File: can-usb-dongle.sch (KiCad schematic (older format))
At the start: 42 parts, among them SW1 SW_PUSH, U1 STM32F302C8T, U2 SN65HVD256, U3 NUF2042XV6, U4 MCP1700, U5 SiP32431, X1 16MHz 10ppm

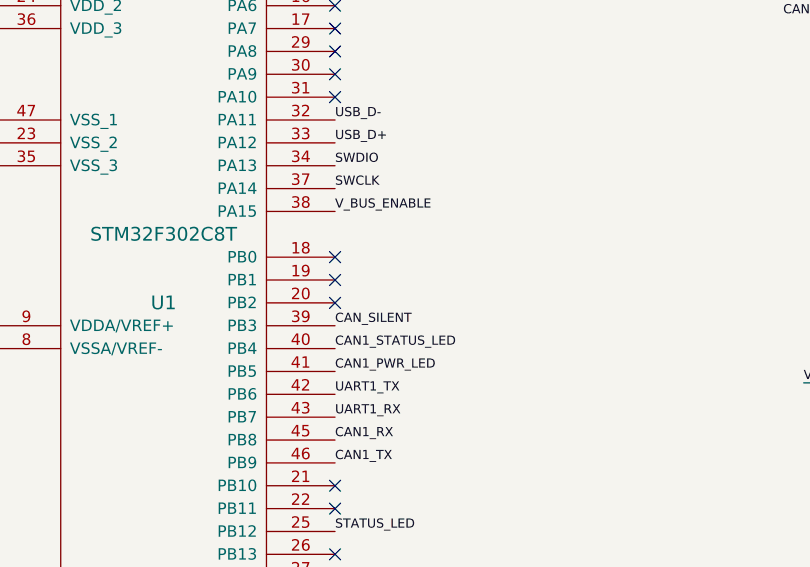
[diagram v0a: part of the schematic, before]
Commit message: Resolve GPIO conflict with JTAG pin
V_BUS_ENABLE and CAN_SILENT were in conflict with JTAG output pins.
They had to be moved because at boot time the output value cannot be guaranteed.
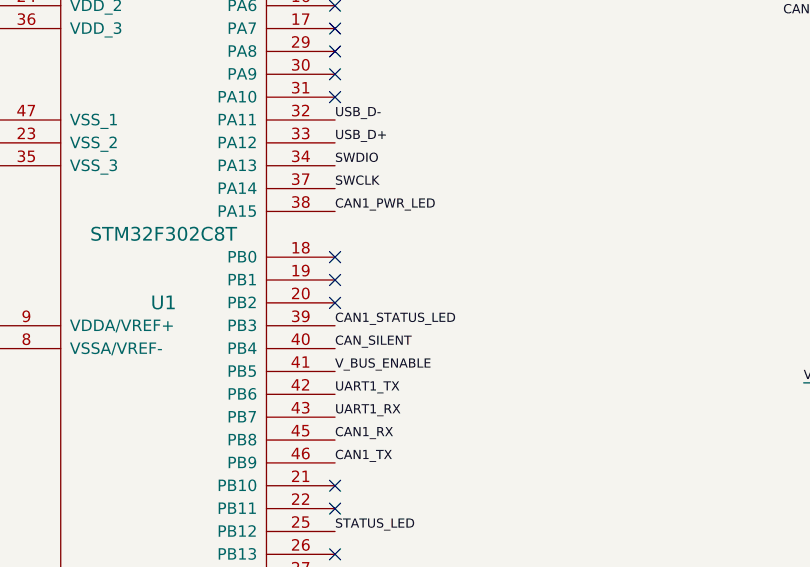
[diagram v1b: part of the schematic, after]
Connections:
- net CAN1_PWR_LED: now also U1.38 (PA15); no longer U1.41 (PB5)
- net CAN1_STATUS_LED: now also U1.39 (PB3); no longer U1.40 (PB4)
- net CAN_SILENT: now also U1.40 (PB4); no longer U1.39 (PB3)
- net V_BUS_ENABLE: now also U1.41 (PB5); no longer U1.38 (PA15)
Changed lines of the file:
@@
 Text Label 6000 1450 2    40   ~ 0
 STATUS_LED
-Text Label 3600 3500 0    40   ~ 0
+Text Label 3600 3400 0    40   ~ 0
 CAN1_STATUS_LED
 $Comp
@@
 	1    0    0    -1
 $EndComp
-Text Label 3600 3400 0    40   ~ 0
+Text Label 3600 3500 0    40   ~ 0
 CAN_SILENT
 Text Label 3600 3800 0    40   ~ 0
@@
 Text Label 8100 2250 0    40   ~ 0
 V_BUS_ENABLE
-Text Label 3600 2900 0    40   ~ 0
+Text Label 3600 3600 0    40   ~ 0
 V_BUS_ENABLE
 $Comp
@@
 Text Label 6000 2050 2    40   ~ 0
 CAN1_PWR_LED
-Text Label 3600 3600 0    40   ~ 0
+Text Label 3600 2900 0    40   ~ 0
 CAN1_PWR_LED
 Text Label 6000 1750 2    40   ~ 0

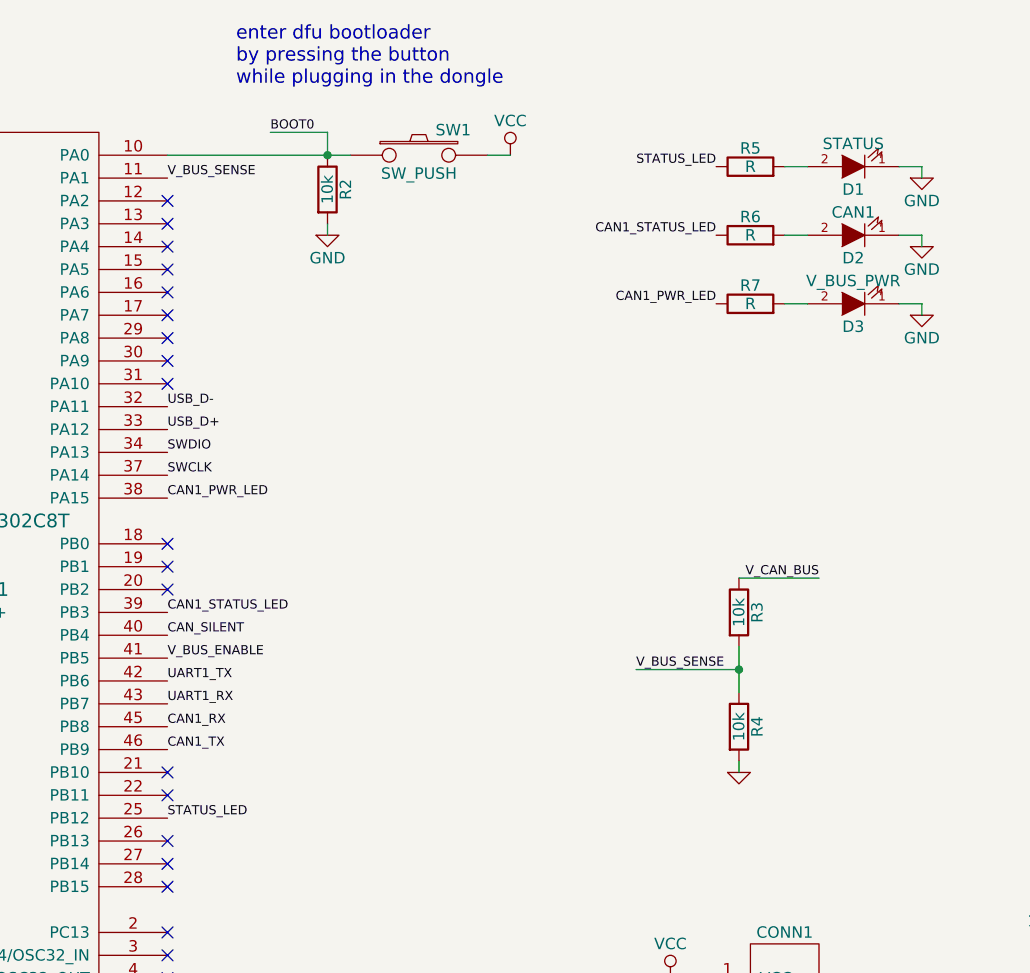
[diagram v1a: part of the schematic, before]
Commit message: Resolve JTAG pin conflict, add V_BUS_SENSE filter cap
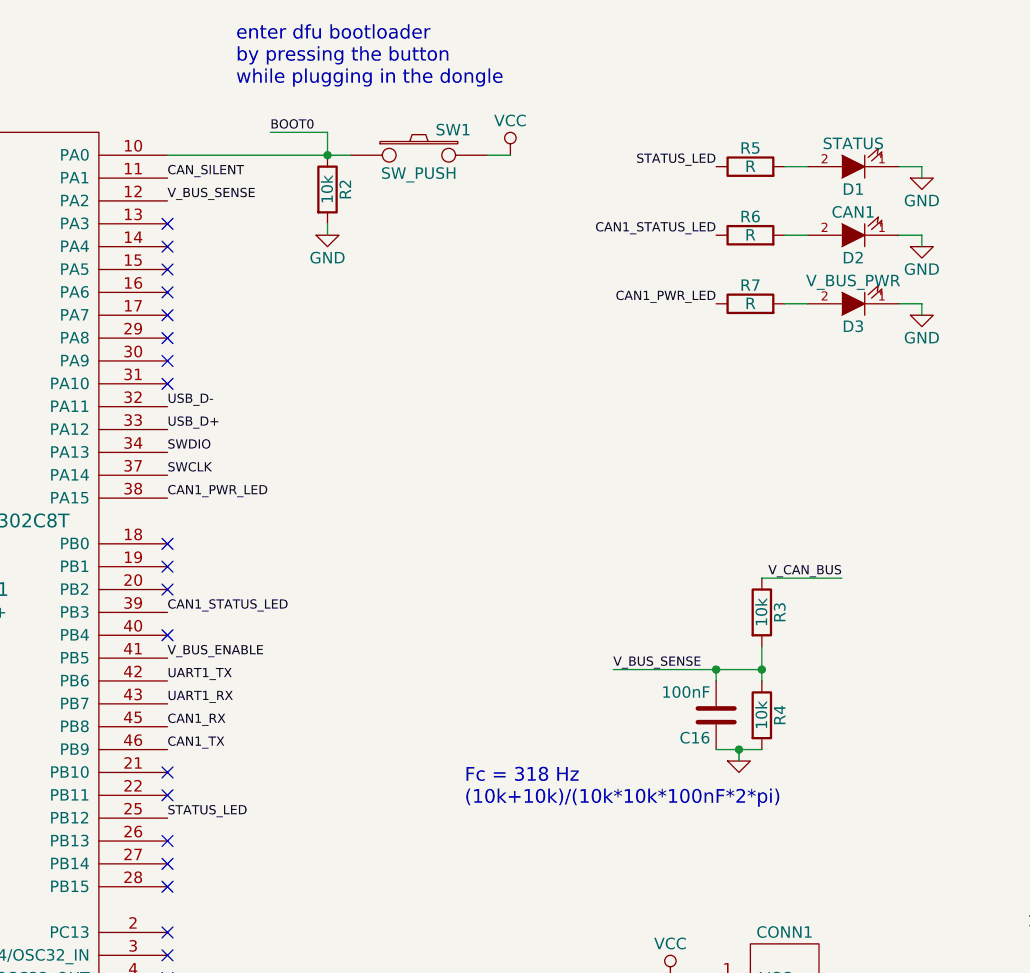
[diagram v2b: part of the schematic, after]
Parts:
- added C16: 100nF, _std:_0603, symbol C
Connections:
- net CAN_SILENT: now also U1.11 (PA1); no longer U1.40 (PB4)
- net GND: now also C16.1
- net V_BUS_SENSE: now also U1.12 (PA2), C16.2; no longer U1.11 (PA1)
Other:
- note added: "Fc = 318 Hz\n(10k+10k)/(10k*10k*100nF*2*pi)"
- moved on the sheet: R3, R4
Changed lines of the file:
@@
 	1    0    0    -1
 $EndComp
-Text Label 3600 3500 0    40   ~ 0
+Text Label 3600 1500 0    40   ~ 0
 CAN_SILENT
 Text Label 3600 3800 0    40   ~ 0
@@
 NoConn ~ 3600 2300
 NoConn ~ 3600 1700
-NoConn ~ 3600 1600
 $Comp
 L CAN CONN5
@@
 	1    0    0    -1
 $EndComp
-Text Label 6450 3250 2    40   ~ 0
+Text Label 6550 3250 2    40   ~ 0
 V_CAN_BUS
 $Comp
 L R R3
 U 1 1 560BE6FC
-P 6100 3400
-F 0 "R3" V 6180 3400 50  0000 C CNN
-F 1 "10k" V 6100 3400 50  0000 C CNN
-F 2 "_std:_0603" V 6030 3400 30  0001 C CNN
-F 3 "" H 6100 3400 30  0000 C CNN
-	1    6100 3400
+P 6200 3400
+F 0 "R3" V 6280 3400 50  0000 C CNN
+F 1 "10k" V 6200 3400 50  0000 C CNN
+F 2 "_std:_0603" V 6130 3400 30  0001 C CNN
+F 3 "" H 6200 3400 30  0000 C CNN
+	1    6200 3400
 	1    0    0    -1
 $EndComp
@@
 L R R4
 U 1 1 560BE79F
-P 6100 3900
-F 0 "R4" V 6180 3900 50  0000 C CNN
-F 1 "10k" V 6100 3900 50  0000 C CNN
-F 2 "_std:_0603" V 6030 3900 30  0001 C CNN
-F 3 "" H 6100 3900 30  0000 C CNN
-	1    6100 3900
+P 6200 3850
+F 0 "R4" V 6280 3850 50  0000 C CNN
+F 1 "10k" V 6200 3850 50  0000 C CNN
+F 2 "_std:_0603" V 6130 3850 30  0001 C CNN
+F 3 "" H 6200 3850 30  0000 C CNN
+	1    6200 3850
 	1    0    0    -1
 $EndComp
@@
 L GND-RESCUE-can-usb-dongle #PWR026
 U 1 1 560BE823
-P 6100 4100
-F 0 "#PWR026" H 6100 4100 30  0001 C CNN
-F 1 "GND" H 6100 4030 30  0001 C CNN
-F 2 "" H 6100 4100 60  0000 C CNN
-F 3 "" H 6100 4100 60  0000 C CNN
-	1    6100 4100
-	1    0    0    -1
-$EndComp
-Text Label 5650 3650 0    40   ~ 0
+P 6100 4050
+F 0 "#PWR026" H 6100 4050 30  0001 C CNN
+F 1 "GND" H 6100 3980 30  0001 C CNN
+F 2 "" H 6100 4050 60  0000 C CNN
+F 3 "" H 6100 4050 60  0000 C CNN
+	1    6100 4050
+	1    0    0    -1
+$EndComp
+Text Label 5550 3650 0    40   ~ 0
 V_BUS_SENSE
-Text Label 3600 1500 0    40   ~ 0
+Text Label 3600 1600 0    40   ~ 0
 V_BUS_SENSE
 $Comp
@@
 Connection ~ 9450 5050
 Wire Wire Line
-	5650 3650 6100 3650
-Wire Wire Line
-	6100 3550 6100 3750
-Connection ~ 6100 3650
-Wire Wire Line
-	6100 4100 6100 4050
-Wire Wire Line
-	6450 3250 6100 3250
+	5550 3650 6200 3650
+Wire Wire Line
+	6200 3550 6200 3700
+Connection ~ 6200 3650
+Wire Wire Line
+	6100 4050 6100 4000
+Wire Wire Line
+	6550 3250 6200 3250
 Wire Wire Line
 	7650 3800 8200 3800
@@
 Text Label 7450 4950 0    40   ~ 0
 V_USB
+NoConn ~ 3600 3500
+$Comp
+L C C16
+U 1 1 562C136A
+P 6000 3850
+F 0 "C16" H 6025 3950 50  0000 L CNN
+F 1 "100nF" H 6025 3750 50  0000 L CNN
+F 2 "_std:_0603" H 6038 3700 30  0001 C CNN
+F 3 "" H 6000 3850 60  0000 C CNN
+	1    6000 3850
+	-1   0    0    1
+$EndComp
+Wire Wire Line
+	6000 3650 6000 3700
+Connection ~ 6000 3650
+Wire Wire Line
+	6000 4000 6200 4000
+Connection ~ 6100 4000
+Text Notes 4900 4250 0    60   ~ 0
+Fc = 318 Hz\n(10k+10k)/(10k*10k*100nF*2*pi)
 $EndSCHEMATC

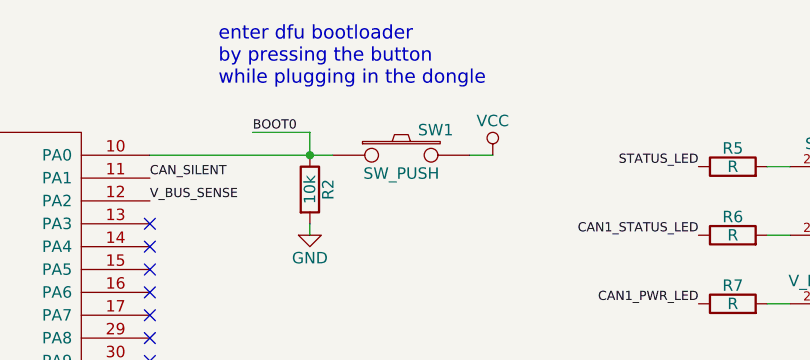
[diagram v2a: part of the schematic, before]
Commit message: Increase component dinstance on backside for handsoldering
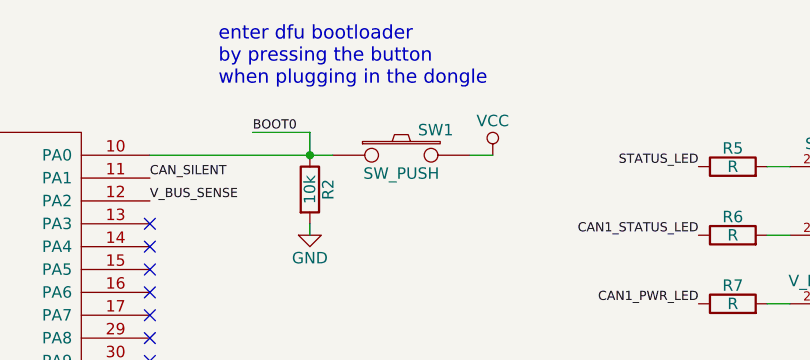
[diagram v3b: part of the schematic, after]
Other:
- note added: "enter dfu bootloader\nby pressing the button\nwhen plugging in the dongle"
- note removed: "enter dfu bootloader\nby pressing the button\nwhile plugging in the dongle"
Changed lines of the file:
@@
 STATUS_LED
 Text Notes 3900 1100 0    60   ~ 0
-enter dfu bootloader\nby pressing the button\nwhile plugging in the dongle
+enter dfu bootloader\nby pressing the button\nwhen plugging in the dongle
 $Comp
 L SiP32431 U5

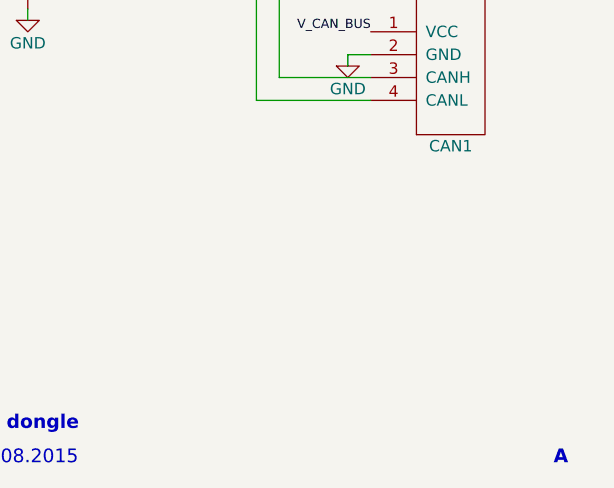
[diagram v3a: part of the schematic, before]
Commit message: Add CVRA logo to schematic
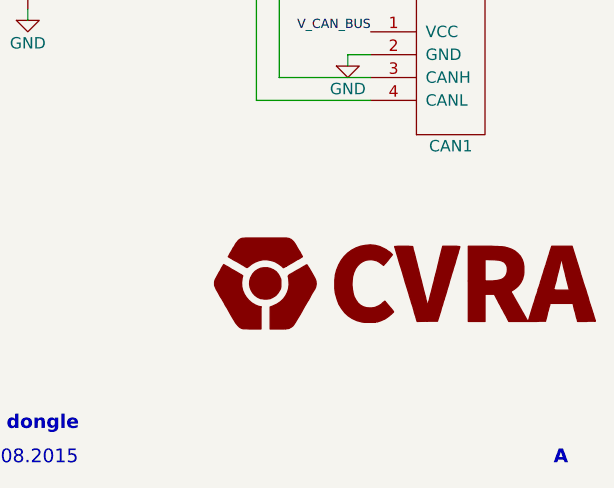
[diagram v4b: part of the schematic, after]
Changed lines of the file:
@@
 LIBS:_power
 LIBS:cvra
+LIBS:logo
 LIBS:can-usb-dongle-cache
 EELAYER 25 0
@@
 $EndDescr
 $Comp
-L GND-RESCUE-can-usb-dongle #PWR01
+L GND-RESCUE-can-usb-dongle #PWR2
 U 1 1 5561F00A
 P 1550 2600
-F 0 "#PWR01" H 1550 2350 50  0001 C CNN
+F 0 "#PWR2" H 1550 2350 50  0001 C CNN
 F 1 "GND" H 1550 2500 50  0000 C CNN
 F 2 "" H 1550 2600 60  0000 C CNN
@@
 $EndComp
 $Comp
-L VCC #PWR02
+L VCC #PWR1
 U 1 1 5561F01F
 P 1550 2150
-F 0 "#PWR02" H 1550 2000 50  0001 C CNN
+F 0 "#PWR1" H 1550 2000 50  0001 C CNN
 F 1 "VCC" H 1550 2300 50  0000 C CNN
 F 2 "" H 1550 2150 60  0000 C CNN
@@
 $EndComp
 $Comp
-L GND-RESCUE-can-usb-dongle #PWR03
+L GND-RESCUE-can-usb-dongle #PWR6
 U 1 1 5561F50D
 P 1850 3650
-F 0 "#PWR03" H 1850 3400 50  0001 C CNN
+F 0 "#PWR6" H 1850 3400 50  0001 C CNN
 F 1 "GND" H 1850 3550 50  0000 C CNN
 F 2 "" H 1850 3650 60  0000 C CNN
@@
 $EndComp
 $Comp
-L VCC #PWR04
+L VCC #PWR5
 U 1 1 5561F52B
 P 1850 3300
-F 0 "#PWR04" H 1850 3150 50  0001 C CNN
+F 0 "#PWR5" H 1850 3150 50  0001 C CNN
 F 1 "VCC" H 1850 3450 50  0000 C CNN
 F 2 "" H 1850 3300 60  0000 C CNN
@@
 $EndComp
 $Comp
-L VCC #PWR05
+L VCC #PWR3
 U 1 1 5561F675
 P 1750 1100
-F 0 "#PWR05" H 1750 950 50  0001 C CNN
+F 0 "#PWR3" H 1750 950 50  0001 C CNN
 F 1 "VCC" H 1750 1250 50  0000 C CNN
 F 2 "" H 1750 1100 60  0000 C CNN
@@
 NRST
 $Comp
-L GND-RESCUE-can-usb-dongle #PWR06
+L GND-RESCUE-can-usb-dongle #PWR11
 U 1 1 556206EF
 P 5400 6800
-F 0 "#PWR06" H 5400 6550 50  0001 C CNN
+F 0 "#PWR11" H 5400 6550 50  0001 C CNN
 F 1 "GND" H 5400 6700 50  0000 C CNN
 F 2 "" H 5400 6800 60  0000 C CNN
@@
 $EndComp
 $Comp
-L VCC #PWR07
+L VCC #PWR10
 U 1 1 55620727
 P 5400 6650
-F 0 "#PWR07" H 5400 6500 50  0001 C CNN
+F 0 "#PWR10" H 5400 6500 50  0001 C CNN
 F 1 "VCC" H 5400 6800 50  0000 C CNN
 F 2 "" H 5400 6650 60  0000 C CNN
@@
 $EndComp
 $Comp
-L GND-RESCUE-can-usb-dongle #PWR08
+L GND-RESCUE-can-usb-dongle #PWR7
 U 1 1 556213D3
 P 4050 5850
-F 0 "#PWR08" H 4050 5600 50  0001 C CNN
+F 0 "#PWR7" H 4050 5600 50  0001 C CNN
 F 1 "GND" H 4050 5750 50  0000 C CNN
 F 2 "" H 4050 5850 60  0000 C CNN
@@
 V_USB
 $Comp
-L GND-RESCUE-can-usb-dongle #PWR09
+L GND-RESCUE-can-usb-dongle #PWR26
 U 1 1 55621D6C
 P 9550 4000
-F 0 "#PWR09" H 9550 3750 50  0001 C CNN
+F 0 "#PWR26" H 9550 3750 50  0001 C CNN
 F 1 "GND" H 9550 3900 50  0000 C CNN
 F 2 "" H 9550 4000 60  0000 C CNN
@@
 $EndComp
 $Comp
-L GND-RESCUE-can-usb-dongle #PWR010
+L GND-RESCUE-can-usb-dongle #PWR4
 U 1 1 5562325F
 P 1750 1750
-F 0 "#PWR010" H 1750 1500 50  0001 C CNN
+F 0 "#PWR4" H 1750 1500 50  0001 C CNN
 F 1 "GND" H 1750 1650 50  0000 C CNN
 F 2 "" H 1750 1750 60  0000 C CNN
@@
 $EndComp
 $Comp
-L GND-RESCUE-can-usb-dongle #PWR011
+L GND-RESCUE-can-usb-dongle #PWR16
 U 1 1 55623201
 P 6900 1800
-F 0 "#PWR011" H 6900 1550 50  0001 C CNN
+F 0 "#PWR16" H 6900 1550 50  0001 C CNN
 F 1 "GND" H 6900 1700 50  0000 C CNN
 F 2 "" H 6900 1800 60  0000 C CNN
@@
 $EndComp
 $Comp
-L GND-RESCUE-can-usb-dongle #PWR012
+L GND-RESCUE-can-usb-dongle #PWR15
 U 1 1 55624280
 P 6900 1500
-F 0 "#PWR012" H 6900 1250 50  0001 C CNN
+F 0 "#PWR15" H 6900 1250 50  0001 C CNN
 F 1 "GND" H 6900 1400 50  0000 C CNN
 F 2 "" H 6900 1500 60  0000 C CNN
@@
 $EndComp
 $Comp
-L GND-RESCUE-can-usb-dongle #PWR013
+L GND-RESCUE-can-usb-dongle #PWR8
 U 1 1 55624C2B
 P 4300 1750
-F 0 "#PWR013" H 4300 1500 50  0001 C CNN
+F 0 "#PWR8" H 4300 1500 50  0001 C CNN
 F 1 "GND" H 4300 1650 50  0000 C CNN
 F 2 "" H 4300 1750 60  0000 C CNN
@@
 $EndComp
 $Comp
-L VCC #PWR014
+L VCC #PWR9
 U 1 1 55624C5D
 P 5100 1400
-F 0 "#PWR014" H 5100 1250 50  0001 C CNN
+F 0 "#PWR9" H 5100 1250 50  0001 C CNN
 F 1 "VCC" H 5100 1550 50  0000 C CNN
 F 2 "" H 5100 1400 60  0000 C CNN
@@
 UART1_RX
 $Comp
-L GND-RESCUE-can-usb-dongle #PWR015
+L GND-RESCUE-can-usb-dongle #PWR13
 U 1 1 55629057
 P 5800 5100
-F 0 "#PWR015" H 5800 4850 50  0001 C CNN
+F 0 "#PWR13" H 5800 4850 50  0001 C CNN
 F 1 "GND" H 5700 5150 50  0000 C CNN
 F 2 "" H 5800 5100 60  0000 C CNN
@@
 V_CAN_BUS
 $Comp
-L VCC #PWR016
+L VCC #PWR12
 U 1 1 5562945D
 P 5800 5000
-F 0 "#PWR016" H 5800 4850 50  0001 C CNN
+F 0 "#PWR12" H 5800 4850 50  0001 C CNN
 F 1 "VCC" H 5800 5150 50  0000 C CNN
 F 2 "" H 5800 5000 60  0000 C CNN
@@
 $EndComp
 $Comp
-L GND-RESCUE-can-usb-dongle #PWR017
+L GND-RESCUE-can-usb-dongle #PWR22
 U 1 1 5592AFB3
 P 8450 5700
-F 0 "#PWR017" H 8450 5450 50  0001 C CNN
+F 0 "#PWR22" H 8450 5450 50  0001 C CNN
 F 1 "GND" H 8450 5600 50  0000 C CNN
 F 2 "" H 8450 5700 60  0000 C CNN
@@
 $EndComp
 $Comp
-L VCC #PWR018
+L VCC #PWR18
 U 1 1 5592BB1F
 P 7300 5250
-F 0 "#PWR018" H 7300 5100 50  0001 C CNN
+F 0 "#PWR18" H 7300 5100 50  0001 C CNN
 F 1 "VCC" H 7300 5400 50  0000 C CNN
 F 2 "" H 7300 5250 60  0000 C CNN
@@
 CAN_SILENT
 $Comp
-L GND-RESCUE-can-usb-dongle #PWR019
+L GND-RESCUE-can-usb-dongle #PWR27
 U 1 1 5592D611
 P 9850 4900
-F 0 "#PWR019" H 9850 4650 50  0001 C CNN
+F 0 "#PWR27" H 9850 4650 50  0001 C CNN
 F 1 "GND" H 9850 4800 50  0000 C CNN
 F 2 "" H 9850 4900 60  0000 C CNN
@@
 $EndComp
 $Comp
-L GND-RESCUE-can-usb-dongle #PWR020
+L GND-RESCUE-can-usb-dongle #PWR24
 U 1 1 55D302BE
 P 9250 1550
-F 0 "#PWR020" H 9250 1300 50  0001 C CNN
+F 0 "#PWR24" H 9250 1300 50  0001 C CNN
 F 1 "GND" H 9250 1450 50  0000 C CNN
 F 2 "" H 9250 1550 60  0000 C CNN
@@
 $EndComp
 $Comp
-L VCC #PWR021
+L VCC #PWR30
 U 1 1 55D305F4
 P 10000 1150
-F 0 "#PWR021" H 10000 1000 50  0001 C CNN
+F 0 "#PWR30" H 10000 1000 50  0001 C CNN
 F 1 "VCC" H 10000 1300 50  0000 C CNN
 F 2 "" H 10000 1150 60  0000 C CNN
@@
 V_CAN_BUS
 $Comp
-L GND-RESCUE-can-usb-dongle #PWR022
+L GND-RESCUE-can-usb-dongle #PWR25
 U 1 1 55D31885
 P 9350 2500
-F 0 "#PWR022" H 9350 2250 50  0001 C CNN
+F 0 "#PWR25" H 9350 2250 50  0001 C CNN
 F 1 "GND" H 9350 2400 50  0000 C CNN
 F 2 "" H 9350 2500 60  0000 C CNN
@@
 $EndComp
 $Comp
-L GND-RESCUE-can-usb-dongle #PWR023
+L GND-RESCUE-can-usb-dongle #PWR23
 U 1 1 55D3211F
 P 8650 2600
-F 0 "#PWR023" H 8650 2350 50  0001 C CNN
+F 0 "#PWR23" H 8650 2350 50  0001 C CNN
 F 1 "GND" H 8650 2500 50  0000 C CNN
 F 2 "" H 8650 2600 60  0000 C CNN
@@
 V_CAN_BUS
 $Comp
-L GND-RESCUE-can-usb-dongle #PWR024
+L GND-RESCUE-can-usb-dongle #PWR28
 U 1 1 55D47D26
 P 9850 5900
-F 0 "#PWR024" H 9850 5650 50  0001 C CNN
+F 0 "#PWR28" H 9850 5650 50  0001 C CNN
 F 1 "GND" H 9850 5800 50  0000 C CNN
 F 2 "" H 9850 5900 60  0000 C CNN
@@
 $EndComp
 $Comp
-L GND-RESCUE-can-usb-dongle #PWR025
+L GND-RESCUE-can-usb-dongle #PWR17
 U 1 1 560BDAA6
 P 6900 2100
-F 0 "#PWR025" H 6900 1850 50  0001 C CNN
+F 0 "#PWR17" H 6900 1850 50  0001 C CNN
 F 1 "GND" H 6900 2000 50  0000 C CNN
 F 2 "" H 6900 2100 60  0000 C CNN
@@
 $EndComp
 $Comp
-L GND-RESCUE-can-usb-dongle #PWR026
+L GND-RESCUE-can-usb-dongle #PWR14
 U 1 1 560BE823
 P 6100 4050
-F 0 "#PWR026" H 6100 4050 30  0001 C CNN
+F 0 "#PWR14" H 6100 4050 30  0001 C CNN
 F 1 "GND" H 6100 3980 30  0001 C CNN
 F 2 "" H 6100 4050 60  0000 C CNN
@@
 $EndComp
 $Comp
-L GND-RESCUE-can-usb-dongle #PWR027
+L GND-RESCUE-can-usb-dongle #PWR29
 U 1 1 560BFB76
 P 9900 3100
-F 0 "#PWR027" H 9900 3100 30  0001 C CNN
+F 0 "#PWR29" H 9900 3100 30  0001 C CNN
 F 1 "GND" H 9900 3030 30  0001 C CNN
 F 2 "" H 9900 3100 60  0000 C CNN
@@
 $EndComp
 $Comp
-L VCC #PWR028
+L VCC #PWR20
 U 1 1 560C391D
 P 8050 3150
-F 0 "#PWR028" H 8050 3250 30  0001 C CNN
+F 0 "#PWR20" H 8050 3250 30  0001 C CNN
 F 1 "VCC" H 8050 3250 30  0000 C CNN
 F 2 "" H 8050 3150 60  0000 C CNN
@@
 $EndComp
 $Comp
-L GND-RESCUE-can-usb-dongle #PWR029
+L GND-RESCUE-can-usb-dongle #PWR21
 U 1 1 560ED3C8
 P 8150 2050
-F 0 "#PWR029" H 8150 2050 30  0001 C CNN
+F 0 "#PWR21" H 8150 2050 30  0001 C CNN
 F 1 "GND" H 8150 1980 30  0001 C CNN
 F 2 "" H 8150 2050 60  0000 C CNN
@@
 $EndComp
 $Comp
-L GND-RESCUE-can-usb-dongle #PWR030
+L GND-RESCUE-can-usb-dongle #PWR31
 U 1 1 560ED852
 P 10000 2250
-F 0 "#PWR030" H 10000 2250 30  0001 C CNN
+F 0 "#PWR31" H 10000 2250 30  0001 C CNN
 F 1 "GND" H 10000 2180 30  0001 C CNN
 F 2 "" H 10000 2250 60  0000 C CNN
@@
 $EndComp
 $Comp
-L GND-RESCUE-can-usb-dongle #PWR031
+L GND-RESCUE-can-usb-dongle #PWR19
 U 1 1 560F050D
 P 7600 4800
-F 0 "#PWR031" H 7600 4800 30  0001 C CNN
+F 0 "#PWR19" H 7600 4800 30  0001 C CNN
 F 1 "GND" H 7600 4730 30  0001 C CNN
 F 2 "" H 7600 4800 60  0000 C CNN
@@
 Text Notes 4900 4250 0    60   ~ 0
 Fc = 318 Hz\n(10k+10k)/(10k*10k*100nF*2*pi)
+$Comp
+L CVRA_logo #G1
+U 1 1 562D3733
+P 10100 6850
+F 0 "#G1" H 10100 6682 60  0001 C CNN
+F 1 "CVRA_logo" H 10100 7018 60  0001 C CNN
+F 2 "" H 10100 6850 60  0000 C CNN
+F 3 "" H 10100 6850 60  0000 C CNN
+	1    10100 6850
+	1    0    0    -1
+$EndComp
 $EndSCHEMATC

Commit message: Update schematic date
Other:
- note added: "25.10.2015"
- note added: "Author: Michael Spieler"
- note removed: "19.08.2015"
- note removed: "Author: Michael Spieler\nReview: -"
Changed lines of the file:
@@
 A
 Text Notes 8200 7650 0    60   ~ 0
-19.08.2015
+25.10.2015
 Text Notes 7050 7100 0    60   ~ 0
-Author: Michael Spieler\nReview: -
+Author: Michael Spieler
 $Comp
 L LED D3
